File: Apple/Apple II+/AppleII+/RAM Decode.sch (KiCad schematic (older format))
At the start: 10 parts, among them Q5 2N3904

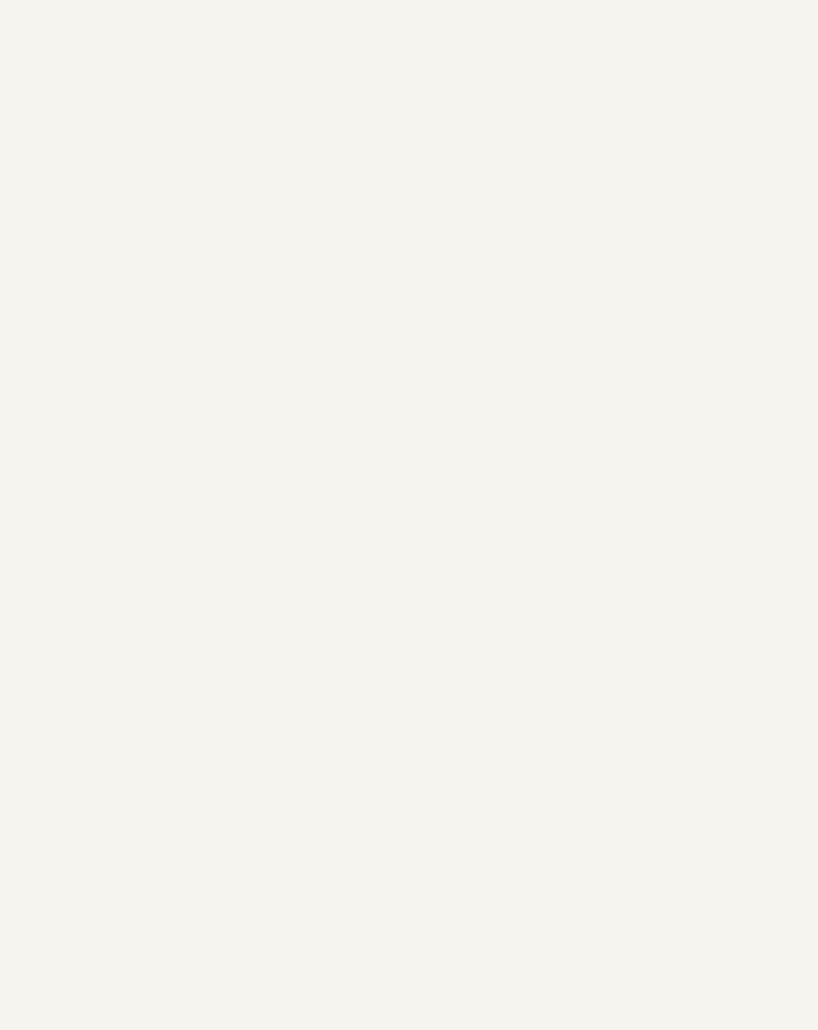
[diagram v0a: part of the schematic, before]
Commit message: Added clock generator sheet, halfway thru it
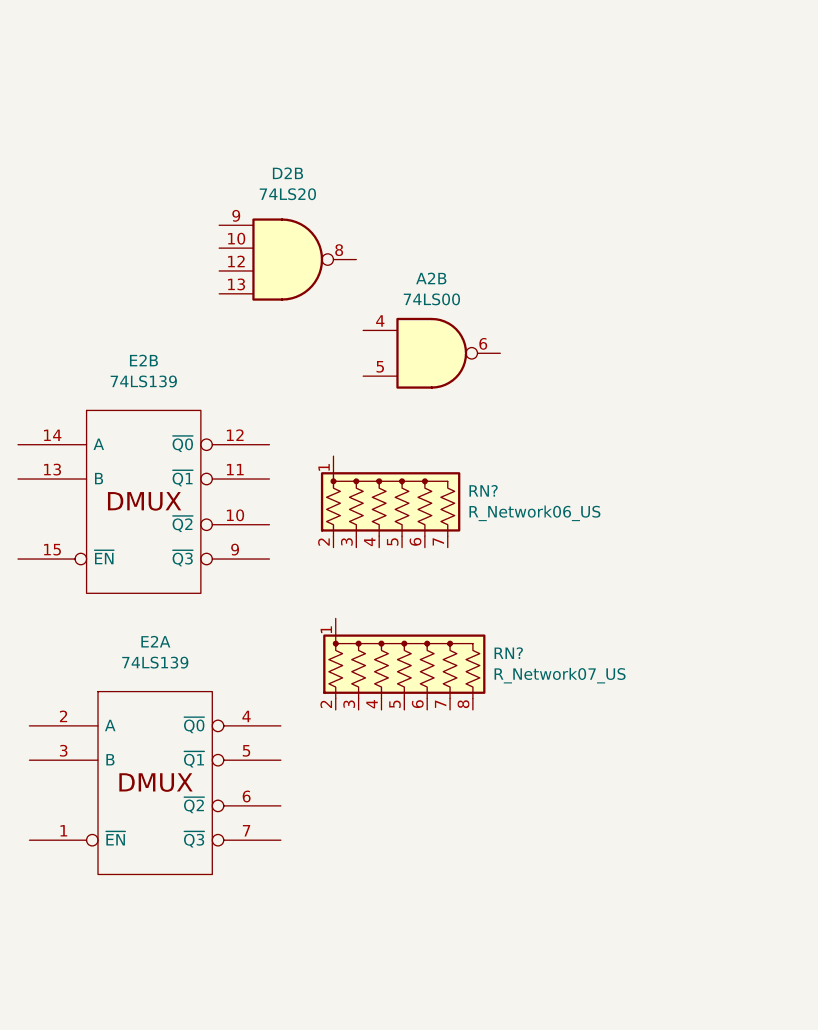
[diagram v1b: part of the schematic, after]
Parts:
- added A2: 74LS00, symbol 74xx:74LS00
- added D2: 74LS20, symbol 74xx:74LS20
- added E2: 74LS139, symbol 74xx_IEEE:74LS139
- added RN?: R_Network06_US, Resistor_THT:R_Array_SIP7, symbol Device:R_Network06_US
- added RN?: R_Network07_US, Resistor_THT:R_Array_SIP8, symbol Device:R_Network07_US
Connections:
- net GND: now also E2.8 (GND), E2.8 (GND)
- new net VCC: E2.16 (VCC), E2.16 (VCC)
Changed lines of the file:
@@
 $Descr A4 11693 8268
 encoding utf-8
-Sheet 7 7
+Sheet 7 8
 Title ""
 Date ""
@@
 Wire Bus Line
 	8870 800  8870 1800
+$Comp
+L Device:R_Network06_US RN?
+U 1 1 60160226
+P 2300 4170
+F 0 "RN?" H 2588 4216 50  0000 L CNN
+F 1 "R_Network06_US" H 2588 4125 50  0000 L CNN
+F 2 "Resistor_THT:R_Array_SIP7" V 2675 4170 50  0001 C CNN
+F 3 "http://www.vishay.com/docs/31509/csc.pdf" H 2300 4170 50  0001 C CNN
+	1    2300 4170
+	1    0    0    -1
+$EndComp
+$Comp
+L Device:R_Network07_US RN?
+U 1 1 60161A23
+P 2310 4880
+F 0 "RN?" H 2698 4926 50  0000 L CNN
+F 1 "R_Network07_US" H 2698 4835 50  0000 L CNN
+F 2 "Resistor_THT:R_Array_SIP8" V 2785 4880 50  0001 C CNN
+F 3 "http://www.vishay.com/docs/31509/csc.pdf" H 2310 4880 50  0001 C CNN
+	1    2310 4880
+	1    0    0    -1
+$EndComp
+$Comp
+L 74xx:74LS00 A2
+U 2 1 60163316
+P 2430 3520
+F 0 "A2" H 2430 3845 50  0000 C CNN
+F 1 "74LS00" H 2430 3754 50  0000 C CNN
+F 2 "" H 2430 3520 50  0001 C CNN
+F 3 "http://www.ti.com/lit/gpn/sn74ls00" H 2430 3520 50  0001 C CNN
+	2    2430 3520
+	1    0    0    -1
+$EndComp
+$Comp
+L 74xx:74LS20 D2
+U 2 1 601652F5
+P 1800 3110
+F 0 "D2" H 1800 3485 50  0000 C CNN
+F 1 "74LS20" H 1800 3394 50  0000 C CNN
+F 2 "" H 1800 3110 50  0001 C CNN
+F 3 "http://www.ti.com/lit/gpn/sn74LS20" H 1800 3110 50  0001 C CNN
+	2    1800 3110
+	1    0    0    -1
+$EndComp
+$Comp
+L 74xx_IEEE:74LS139 E2
+U 2 1 601683CD
+P 1170 4170
+F 0 "E2" H 1170 4786 50  0000 C CNN
+F 1 "74LS139" H 1170 4695 50  0000 C CNN
+F 2 "" H 1170 4170 50  0001 C CNN
+F 3 "http://www.ti.com/lit/ds/symlink/sn74ls139a.pdf" H 1170 4170 50  0001 C CNN
+	2    1170 4170
+	1    0    0    -1
+$EndComp
+$Comp
+L 74xx_IEEE:74LS139 E2
+U 1 1 60169CB7
+P 1220 5400
+F 0 "E2" H 1220 6016 50  0000 C CNN
+F 1 "74LS139" H 1220 5925 50  0000 C CNN
+F 2 "" H 1220 5400 50  0001 C CNN
+F 3 "http://www.ti.com/lit/ds/symlink/sn74ls139a.pdf" H 1220 5400 50  0001 C CNN
+	1    1220 5400
+	1    0    0    -1
+$EndComp
 $EndSCHEMATC

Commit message: Added video generation sheet
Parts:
- removed A13: 555, digikey-footprints:DIP-8_W7.62mm, symbol AppleII+:555
- removed A2: 74LS00, symbol 74xx:74LS00
- removed A7: Keyboard_Connector, symbol AppleII+:AppleII+_Keyboard_Connector
- removed B10: 74LS74, symbol 74xx:74LS74
- removed B6, B7: 74LS257, symbol 74xx:74LS257
- removed C11: 74LS04, symbol 74xx:74LS04
- removed C4: .1uF, symbol Device:C_Small
- removed D2: 74LS20, symbol 74xx:74LS20
- removed E2: 74LS139, symbol 74xx_IEEE:74LS139
- removed Q5: 2N3904, Package_TO_SOT_THT:TO-92_Inline, symbol Transistor_BJT:2N3904
- removed R14: 1K, symbol Device:R
- removed R26: 2M2, symbol Device:R
- removed RN?: R_Network06_US, Resistor_THT:R_Array_SIP7, symbol Device:R_Network06_US
- removed RN?: R_Network07_US, Resistor_THT:R_Array_SIP8, symbol Device:R_Network07_US
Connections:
- no-connect marks 3 -> 0
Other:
- note removed: "Power-up reset"
